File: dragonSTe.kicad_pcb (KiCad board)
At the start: 2 copper layers, 130 parts, among them J2 MIDI OUT, J3 MIDI IN, J4 DB25_Socket, J5 DB25_Pins, J6 Keyboard, SW1 RESET, U1 68000, U5 LM555xM, U7 MC6850, U8 MC6850, U9 YM2149, X1 8.010613MHz

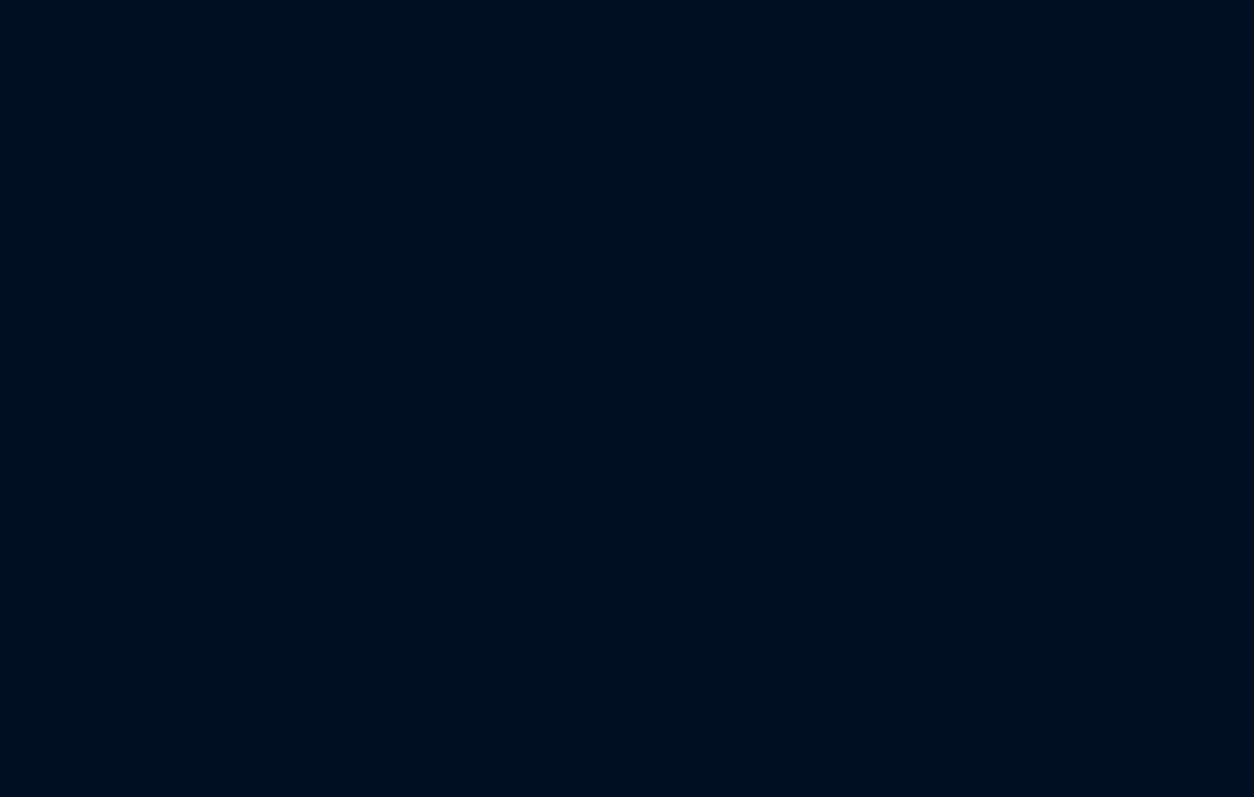
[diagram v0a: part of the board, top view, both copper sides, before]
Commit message: motherboard: Added the HDD and FDD controller logic to the schematic
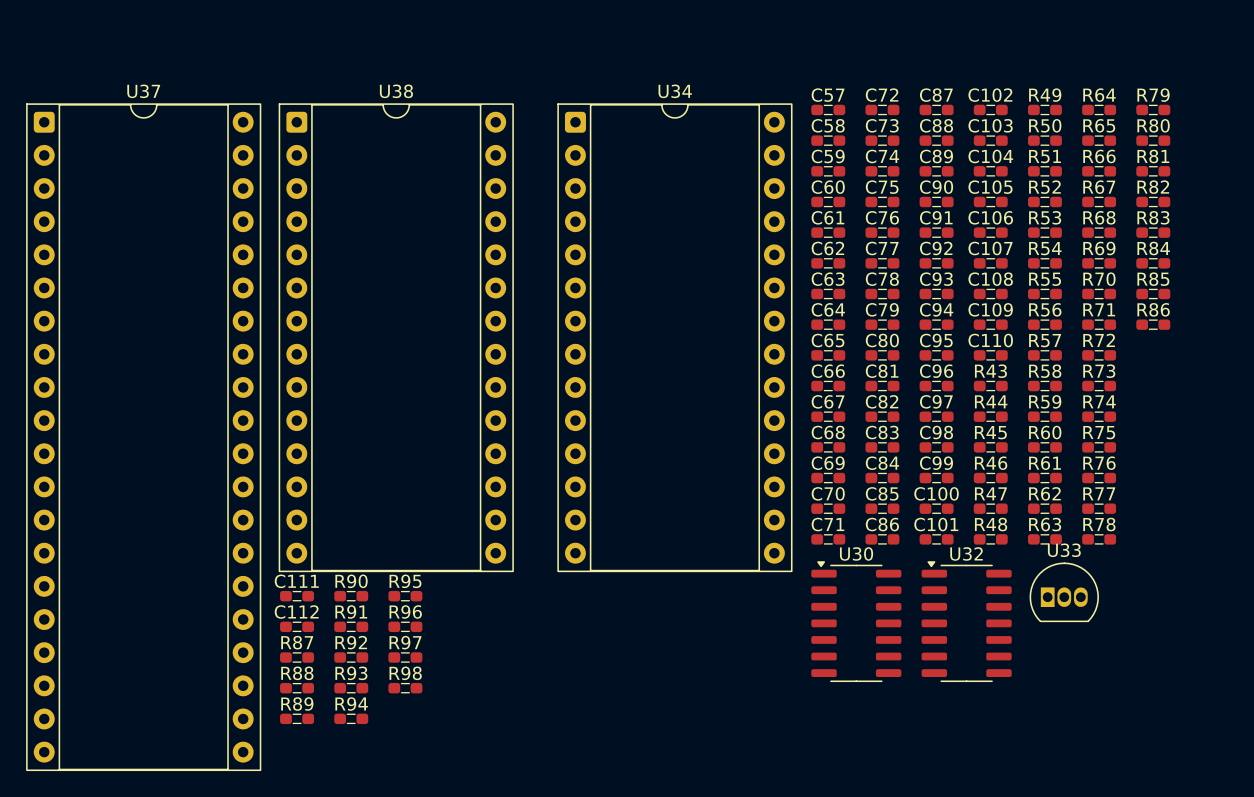
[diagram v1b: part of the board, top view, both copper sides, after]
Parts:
- added C100: 8n2, rhais_rcl:C0603, F.Cu at (156.9, 193.2)
- added C101: 8n2, rhais_rcl:C0603, F.Cu at (156.9, 195.6)
- added C102: 8n2, rhais_rcl:C0603, F.Cu at (161.1, 162.7)
- added C103: 880p, rhais_rcl:C0603, F.Cu at (161.1, 165.0)
- added C104: 880p, rhais_rcl:C0603, F.Cu at (161.1, 167.4)
- added C105: 10n, rhais_rcl:C0603, F.Cu at (161.1, 169.7)
- added C106: 10n, rhais_rcl:C0603, F.Cu at (161.1, 172.1)
- added C107: 10n, rhais_rcl:C0603, F.Cu at (161.1, 174.4)
- added C108: 880p, rhais_rcl:C0603, F.Cu at (161.1, 176.8)
- added C109: 10n, rhais_rcl:C0603, F.Cu at (161.1, 179.1)
- added C110: 880p, rhais_rcl:C0603, F.Cu at (161.1, 181.5)
- added C111: 100n, rhais_rcl:C0603, F.Cu at (108.0, 199.9)
- added C112: 100n, rhais_rcl:C0603, F.Cu at (108.0, 202.3)
- added C57: 100n, rhais_rcl:C0603, F.Cu at (148.7, 162.7)
- added C58: 100n, rhais_rcl:C0603, F.Cu at (148.7, 165.0)
- added C59: 100n, rhais_rcl:C0603, F.Cu at (148.7, 167.4)
- added C60: 100n, rhais_rcl:C0603, F.Cu at (148.7, 169.7)
- added C61: 47u, rhais_rcl:C0603, F.Cu at (148.7, 172.1)
- added C62: 100u, rhais_rcl:C0603, F.Cu at (148.7, 174.4)
- added C63: 100n, rhais_rcl:C0603, F.Cu at (148.7, 176.8)
- added C64: 100u, rhais_rcl:C0603, F.Cu at (148.7, 179.1)
- added C65: 100n, rhais_rcl:C0603, F.Cu at (148.7, 181.5)
- added C66: 10n, rhais_rcl:C0603, F.Cu at (148.7, 183.8)
- added C67: 100n, rhais_rcl:C0603, F.Cu at (148.7, 186.2)
- added C68: 100n, rhais_rcl:C0603, F.Cu at (148.7, 188.5)
- added C69: 100n, rhais_rcl:C0603, F.Cu at (148.7, 190.9)
- added C70: 100n, rhais_rcl:C0603, F.Cu at (148.7, 193.2)
- added C71: 10n, rhais_rcl:C0603, F.Cu at (148.7, 195.6)
- added C72: 100n, rhais_rcl:C0603, F.Cu at (152.8, 162.7)
- added C73: 100n, rhais_rcl:C0603, F.Cu at (152.8, 165.0)
- added C74: 47u, rhais_rcl:C0603, F.Cu at (152.8, 167.4)
- added C75: 1n, rhais_rcl:C0603, F.Cu at (152.8, 169.7)
- added C76: 1n, rhais_rcl:C0603, F.Cu at (152.8, 172.1)
- added C77: 1n, rhais_rcl:C0603, F.Cu at (152.8, 174.4)
- added C78: 1n, rhais_rcl:C0603, F.Cu at (152.8, 176.8)
- added C79: 47u, rhais_rcl:C0603, F.Cu at (152.8, 179.1)
- added C80: 1n, rhais_rcl:C0603, F.Cu at (152.8, 181.5)
- added C81: 1n, rhais_rcl:C0603, F.Cu at (152.8, 183.8)
- added C82: 1n, rhais_rcl:C0603, F.Cu at (152.8, 186.2)
- added C83: 1n, rhais_rcl:C0603, F.Cu at (152.8, 188.5)
- added C84: 47u, rhais_rcl:C0603, F.Cu at (152.8, 190.9)
- added C85: 100n, rhais_rcl:C0603, F.Cu at (152.8, 193.2)
- added C86: 100n, rhais_rcl:C0603, F.Cu at (152.8, 195.6)
- added C87: 47u, rhais_rcl:C0603, F.Cu at (156.9, 162.7)
- added C88: 47u, rhais_rcl:C0603, F.Cu at (156.9, 165.0)
- added C89: 10u, rhais_rcl:C0603, F.Cu at (156.9, 167.4)
- added C90: 47u, rhais_rcl:C0603, F.Cu at (156.9, 169.7)
- added C91: 47u, rhais_rcl:C0603, F.Cu at (156.9, 172.1)
- added C92: 47u, rhais_rcl:C0603, F.Cu at (156.9, 174.4)
- added C93: 47u, rhais_rcl:C0603, F.Cu at (156.9, 176.8)
- added C94: 100n, rhais_rcl:C0603, F.Cu at (156.9, 179.1)
- added C95: 100u, rhais_rcl:C0603, F.Cu at (156.9, 181.5)
- added C96: 100n, rhais_rcl:C0603, F.Cu at (156.9, 183.8)
- added C97: 47u, rhais_rcl:C0603, F.Cu at (156.9, 186.2)
- added C98: 47u, rhais_rcl:C0603, F.Cu at (156.9, 188.5)
- added C99: 8n2, rhais_rcl:C0603, F.Cu at (156.9, 190.9)
- added R43: 10k, rhais_rcl:R0603, F.Cu at (161.1, 183.8)
- added R44: 10k, rhais_rcl:R0603, F.Cu at (161.1, 186.2)
- added R45: 8k2, rhais_rcl:R0603, F.Cu at (161.1, 188.5)
- added R46: 8k2, rhais_rcl:R0603, F.Cu at (161.1, 190.9)
- added R47: 100k, rhais_rcl:R0603, F.Cu at (161.1, 193.2)
- added R48: 10R, rhais_rcl:R0603, F.Cu at (161.1, 195.6)
- added R49: 10R, rhais_rcl:R0603, F.Cu at (165.2, 162.7)
- added R50: 10k, rhais_rcl:R0603, F.Cu at (165.2, 165.0)
- added R51: 10k, rhais_rcl:R0603, F.Cu at (165.2, 167.4)
- added R52: 8k2, rhais_rcl:R0603, F.Cu at (165.2, 169.7)
- added R53: 8k2, rhais_rcl:R0603, F.Cu at (165.2, 172.1)
- added R54: 100k, rhais_rcl:R0603, F.Cu at (165.2, 174.4)
- added R55: 10k, rhais_rcl:R0603, F.Cu at (165.2, 176.8)
- added R56: 10k, rhais_rcl:R0603, F.Cu at (165.2, 179.1)
- added R57: 10k, rhais_rcl:R0603, F.Cu at (165.2, 181.5)
- added R58: 10k, rhais_rcl:R0603, F.Cu at (165.2, 183.8)
- added R59: 1k8, rhais_rcl:R0603, F.Cu at (165.2, 186.2)
- added R60: 10k, rhais_rcl:R0603, F.Cu at (165.2, 188.5)
- added R61: 10k, rhais_rcl:R0603, F.Cu at (165.2, 190.9)
- added R62: 10k, rhais_rcl:R0603, F.Cu at (165.2, 193.2)
- added R63: 10k, rhais_rcl:R0603, F.Cu at (165.2, 195.6)
- added R64: 1k8, rhais_rcl:R0603, F.Cu at (169.4, 162.7)
- added R65: 10k, rhais_rcl:R0603, F.Cu at (169.4, 165.0)
- added R66: 3k6, rhais_rcl:R0603, F.Cu at (169.4, 167.4)
- added R67: 1k, rhais_rcl:R0603, F.Cu at (169.4, 169.7)
- added R68: 10k, rhais_rcl:R0603, F.Cu at (169.4, 172.1)
- added R69: 3k6, rhais_rcl:R0603, F.Cu at (169.4, 174.4)
- added R70: 1k, rhais_rcl:R0603, F.Cu at (169.4, 176.8)
- added R71: 1k, rhais_rcl:R0603, F.Cu at (169.4, 179.1)
- added R72: 1k, rhais_rcl:R0603, F.Cu at (169.4, 181.5)
- added R73: 270k, rhais_rcl:R0603, F.Cu at (169.4, 183.8)
- added R74: 270k, rhais_rcl:R0603, F.Cu at (169.4, 186.2)
- added R75: 51k, rhais_rcl:R0603, F.Cu at (169.4, 188.5)
- added R76: 51k, rhais_rcl:R0603, F.Cu at (169.4, 190.9)
- added R77: 10k, rhais_rcl:R0603, F.Cu at (169.4, 193.2)
- added R78: 10k, rhais_rcl:R0603, F.Cu at (169.4, 195.6)
- added R79: 470R, rhais_rcl:R0603, F.Cu at (173.6, 162.7)
- added R80: 470R, rhais_rcl:R0603, F.Cu at (173.6, 165.0)
- added R81: 1M, rhais_rcl:R0603, F.Cu at (173.6, 167.4)
- added R82: 1M, rhais_rcl:R0603, F.Cu at (173.6, 169.7)
- added R83: 1M, rhais_rcl:R0603, F.Cu at (173.6, 172.1)
- added R84: 470R, rhais_rcl:R0603, F.Cu at (173.6, 174.4)
- added R85: 1M, rhais_rcl:R0603, F.Cu at (173.6, 176.8)
- added R86: 470R, rhais_rcl:R0603, F.Cu at (173.6, 179.1)
- added R87: 1k, rhais_rcl:R0603, F.Cu at (108.0, 204.6)
- added R88: 1k, rhais_rcl:R0603, F.Cu at (108.0, 207.0)
- added R89: 1k, rhais_rcl:R0603, F.Cu at (108.0, 209.3)
- added R90: 1k, rhais_rcl:R0603, F.Cu at (112.1, 199.9)
- added R91: 1k, rhais_rcl:R0603, F.Cu at (112.1, 202.3)
- added R92: 1k, rhais_rcl:R0603, F.Cu at (112.1, 204.6)
- added R93: 1k, rhais_rcl:R0603, F.Cu at (112.1, 207.0)
- added R94: 220R, rhais_rcl:R0603, F.Cu at (112.1, 209.3)
- added R95: 47R, rhais_rcl:R0603, F.Cu at (116.2, 199.9)
- added R96: 47R, rhais_rcl:R0603, F.Cu at (116.2, 202.3)
- added R97: 47R, rhais_rcl:R0603, F.Cu at (116.2, 204.6)
- added R98: 47R, rhais_rcl:R0603, F.Cu at (116.2, 207.0)
- added U30: LF347DT, Package_SO:SO-14_3.9x8.65mm_P1.27mm, F.Cu at (150.8, 202.0)
- added U32: LF347DT, Package_SO:SO-14_3.9x8.65mm_P1.27mm, F.Cu at (159.2, 202.0)
- added U33: LM78L82, Package_TO_SOT_THT:TO-92_Inline, F.Cu at (165.5, 200.0)
- added U34: LMC1992, Package_DIP:DIP-28_W15.24mm_Socket, F.Cu at (129.3, 163.6)
- added U37: DMA, Package_DIP:DIP-40_W15.24mm_Socket, F.Cu at (88.6, 163.6)
- added U38: WD1772, Package_DIP:DIP-28_W15.24mm_Socket, F.Cu at (107.9, 163.6)
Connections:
- net /Disk & DMA/BD0SEL renamed /Disk & Floppy/BD0SEL
- net /Disk & DMA/CLK2 renamed /Disk & Floppy/CLK2
- net /Disk & DMA/D0SEL renamed /Disk & Floppy/D0SEL
- net /Disk & DMA/D1SEL renamed /Disk & Floppy/D1SEL
- net /Disk & DMA/S0SEL renamed /Disk & Floppy/S0SEL
- net Net-(U9-A) renamed /DAC + Joysticks/AUDIOS
- net VCC renamed +5V
- RN13 pad 1: unconnected-(RN13-R1.1-Pad1) -> Net-(RN13-R1.1)
- RN13 pad 2: unconnected-(RN13-R2.1-Pad2) -> Net-(RN13-R2.1)
- RN13 pad 3: unconnected-(RN13-R3.1-Pad3) -> Net-(RN13-R3.1)
- RN13 pad 4: unconnected-(RN13-R4.1-Pad4) -> Net-(RN13-R4.1)
- RN14 pad 1: unconnected-(RN14-R1.1-Pad1) -> Net-(RN14-R1.1)
- RN14 pad 2: unconnected-(RN14-R2.1-Pad2) -> Net-(RN14-R2.1)
- RN14 pad 3: unconnected-(RN14-R3.1-Pad3) -> Net-(RN14-R3.1)
- RN14 pad 4: unconnected-(RN14-R4.1-Pad4) -> Net-(RN14-R4.1)
- RN15 pad 1: unconnected-(RN15-R1.1-Pad1) -> /Disk & Floppy/~{HDCS}
- RN15 pad 2: unconnected-(RN15-R2.1-Pad2) -> /Disk & Floppy/~{HDACK}
- RN15 pad 3: unconnected-(RN15-R3.1-Pad3) -> /Disk & Floppy/HDA0
- RN15 pad 4: unconnected-(RN15-R4.1-Pad4) -> /Disk & Floppy/HDR/~{W}
- X1 pad 3: /Disk & DMA/SCLK -> /Disk & Floppy/SCLK

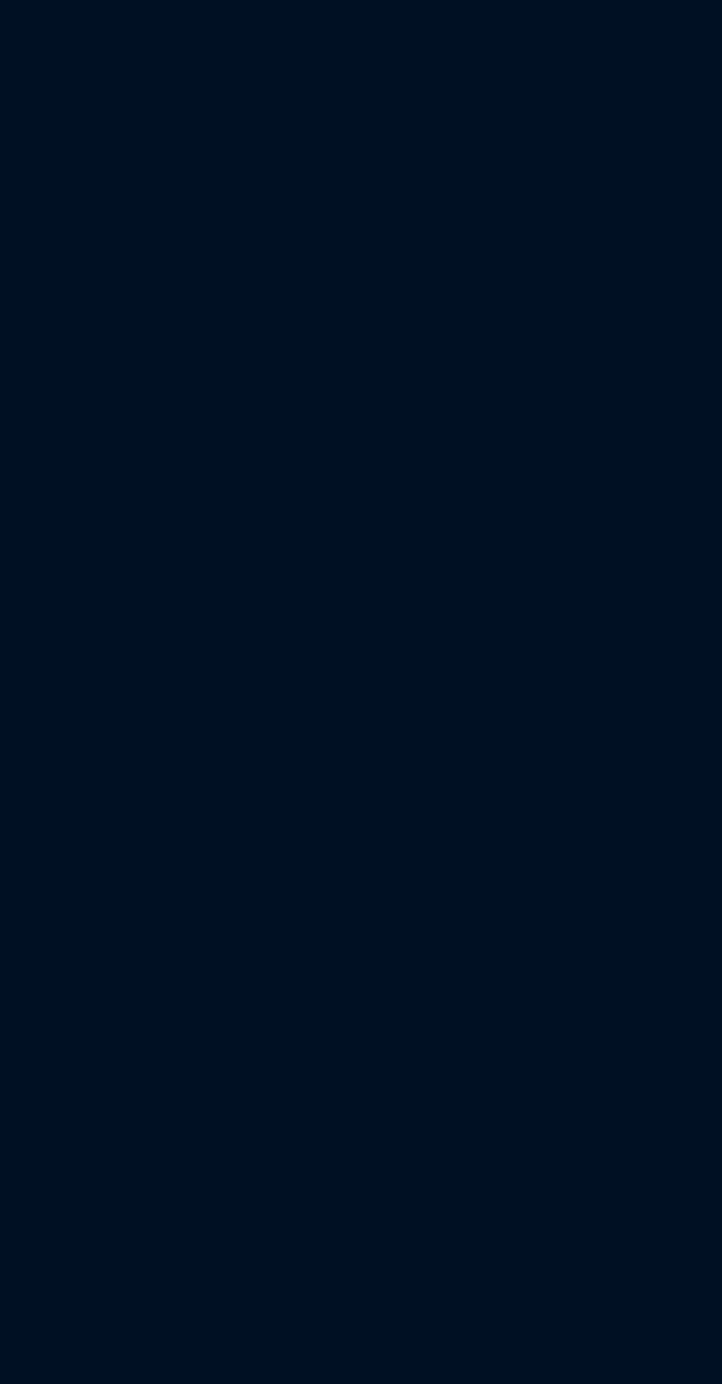
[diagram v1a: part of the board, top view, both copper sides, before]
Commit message: motherboard: Added the BLiTTER to the schematic and tidied up a pile
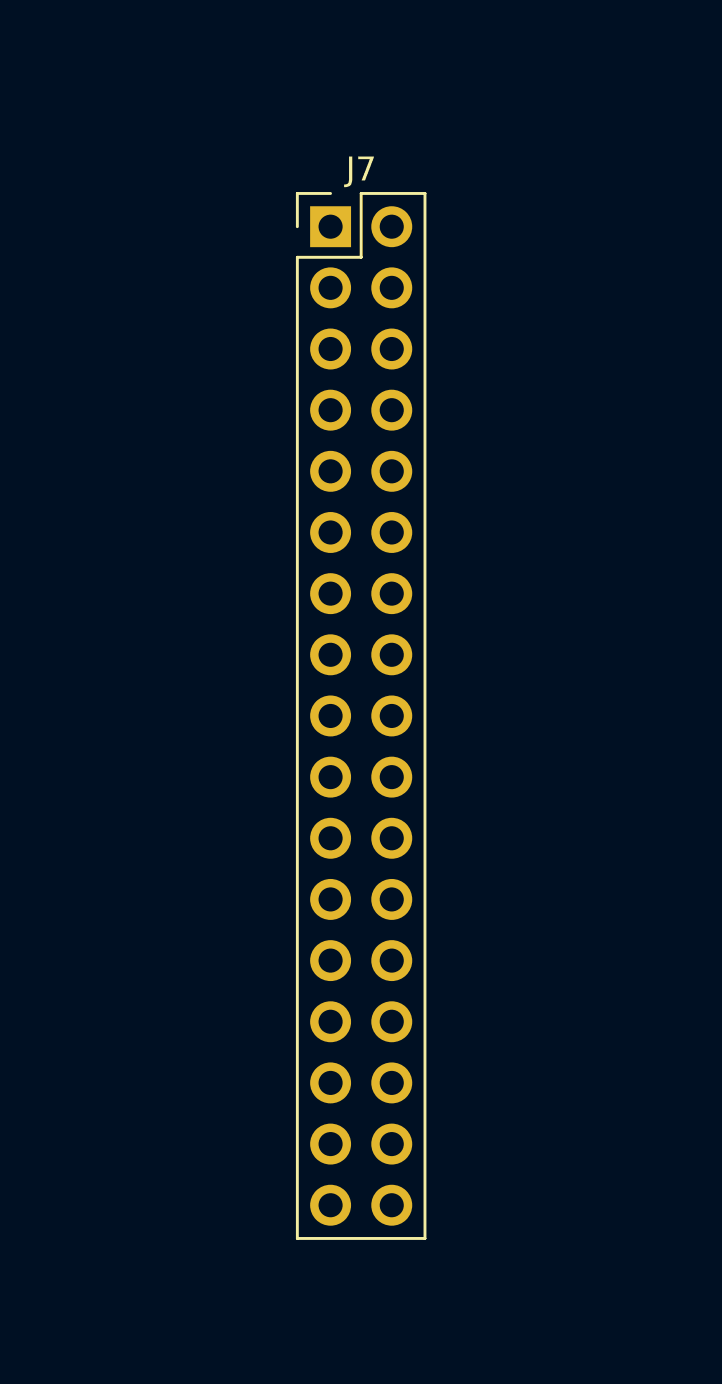
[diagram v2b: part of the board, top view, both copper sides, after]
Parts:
- added J7: Internal FDD, Connector_PinHeader_2.54mm:PinHeader_2x17_P2.54mm_Vertical, F.Cu at (198.7, 157.4)

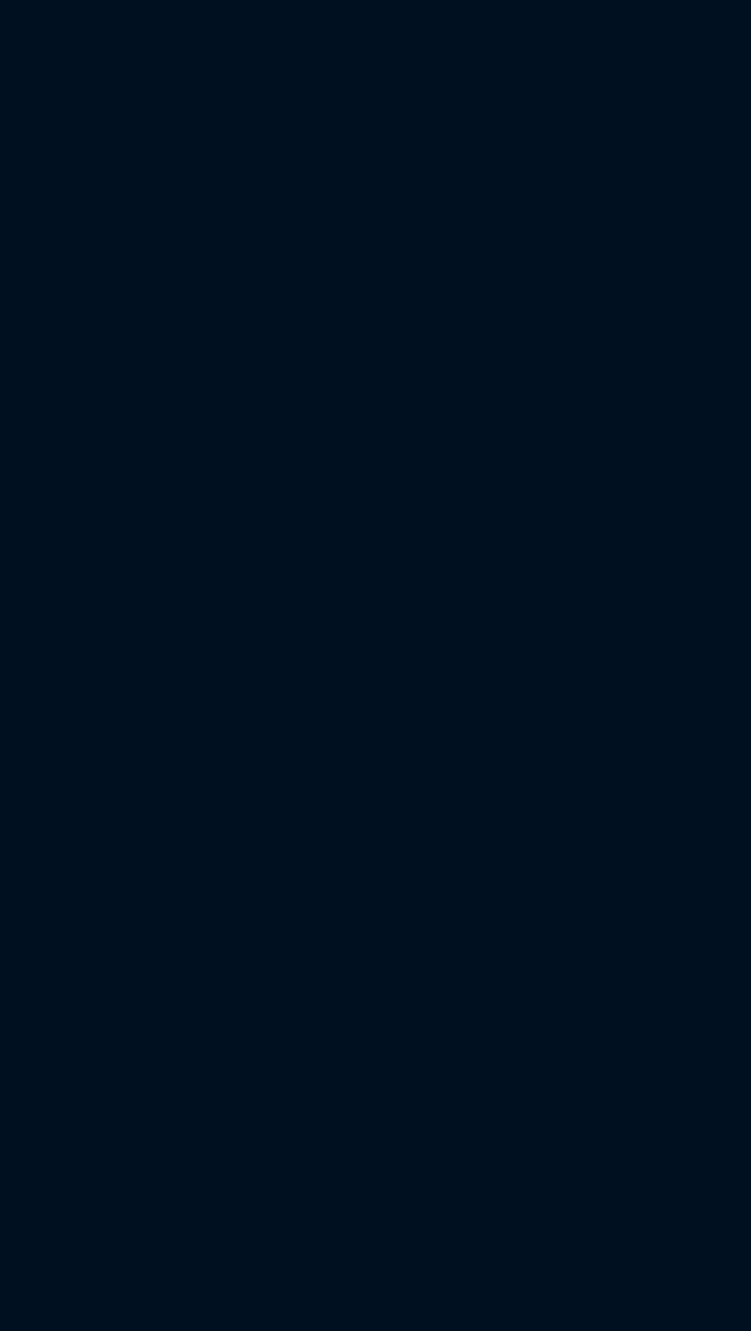
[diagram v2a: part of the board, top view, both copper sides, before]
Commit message: motherboard: Added SHIFTER to the schematic and tidied up a pile
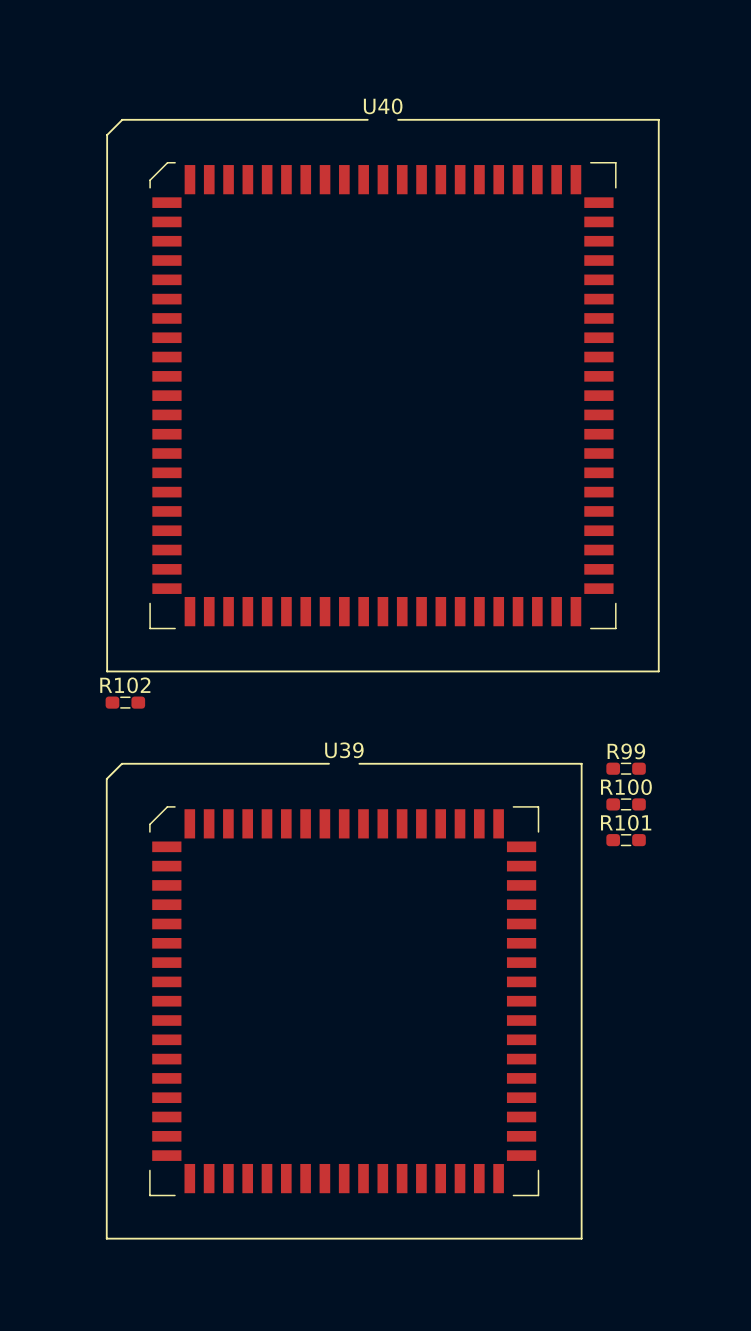
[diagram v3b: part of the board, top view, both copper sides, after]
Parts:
- added R100: 10k, rhais_rcl:R0603, F.Cu at (303.9, 162.2)
- added R101: 10k, rhais_rcl:R0603, F.Cu at (303.9, 164.5)
- added R102: 1k, rhais_rcl:R0603, F.Cu at (270.9, 155.5)
- added R99: 10k, rhais_rcl:R0603, F.Cu at (303.9, 159.8)
- added U39: STB, Package_LCC:PLCC-68_SMD-Socket, F.Cu at (285.3, 175.1)
- added U40: GST_SHIFTER, Package_LCC:PLCC-84_SMD-Socket, F.Cu at (287.9, 135.3)
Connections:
- R34 pad 2: /IO Interfaces/~{BLT_INT} -> /CPU+ROMs/~{BLT_INT}
- U1 pad 11: unconnected-(U1-BG-Pad11) -> /CPU+ROMs/~{CPU_BG}
- U1 pad 26: unconnected-(U1-FC2-Pad26) -> /CPU+ROMs/FC2
- U1 pad 27: unconnected-(U1-FC1-Pad27) -> /CPU+ROMs/FC1
- U1 pad 28: unconnected-(U1-FC0-Pad28) -> /CPU+ROMs/FC0
- U37 pad 1: /CPU+ROMs/SysBus.R/~{W} -> /Disk & Floppy/SysBus.R/~{W}
- U37 pad 12: /CPU+ROMs/SysBus.D8 -> /Disk & Floppy/SysBus.D8
- U37 pad 13: /CPU+ROMs/SysBus.D9 -> /Disk & Floppy/SysBus.D9
- U37 pad 14: /CPU+ROMs/SysBus.D10 -> /Disk & Floppy/SysBus.D10
- U37 pad 15: /CPU+ROMs/SysBus.D11 -> /Disk & Floppy/SysBus.D11
- U37 pad 16: /CPU+ROMs/SysBus.D12 -> /Disk & Floppy/SysBus.D12
- U37 pad 17: /CPU+ROMs/SysBus.D13 -> /Disk & Floppy/SysBus.D13
- U37 pad 18: /CPU+ROMs/SysBus.D14 -> /Disk & Floppy/SysBus.D14
- U37 pad 19: /CPU+ROMs/SysBus.D15 -> /Disk & Floppy/SysBus.D15
- U37 pad 2: /CPU+ROMs/SysBus.A1 -> /Disk & Floppy/SysBus.A1
- U7 pad 11: /CPU+ROMs/SysBus.A1 -> /IO Interfaces/SysBus.A1
- U7 pad 13: /CPU+ROMs/SysBus.R/~{W} -> /IO Interfaces/SysBus.R/~{W}
- U7 pad 14: /CPU+ROMs/SysBus.E -> /IO Interfaces/SysBus.E
- U7 pad 15: /CPU+ROMs/SysBus.D15 -> /IO Interfaces/SysBus.D15
- U7 pad 16: /CPU+ROMs/SysBus.D14 -> /IO Interfaces/SysBus.D14
- U7 pad 17: /CPU+ROMs/SysBus.D13 -> /IO Interfaces/SysBus.D13
- U7 pad 18: /CPU+ROMs/SysBus.D12 -> /IO Interfaces/SysBus.D12
- U7 pad 19: /CPU+ROMs/SysBus.D11 -> /IO Interfaces/SysBus.D11
- U7 pad 20: /CPU+ROMs/SysBus.D10 -> /IO Interfaces/SysBus.D10
- U7 pad 21: /CPU+ROMs/SysBus.D9 -> /IO Interfaces/SysBus.D9
- U7 pad 22: /CPU+ROMs/SysBus.D8 -> /IO Interfaces/SysBus.D8
- U7 pad 9: /CPU+ROMs/SysBus.A2 -> /IO Interfaces/SysBus.A2
- U8 pad 10: /CPU+ROMs/SysBus.A2 -> /IO Interfaces/SysBus.A2
- U8 pad 11: /CPU+ROMs/SysBus.A1 -> /IO Interfaces/SysBus.A1
- U8 pad 13: /CPU+ROMs/SysBus.R/~{W} -> /IO Interfaces/SysBus.R/~{W}
- U8 pad 14: /CPU+ROMs/SysBus.E -> /IO Interfaces/SysBus.E
- U8 pad 15: /CPU+ROMs/SysBus.D15 -> /IO Interfaces/SysBus.D15
- U8 pad 16: /CPU+ROMs/SysBus.D14 -> /IO Interfaces/SysBus.D14
- U8 pad 17: /CPU+ROMs/SysBus.D13 -> /IO Interfaces/SysBus.D13
- U8 pad 18: /CPU+ROMs/SysBus.D12 -> /IO Interfaces/SysBus.D12
- U8 pad 19: /CPU+ROMs/SysBus.D11 -> /IO Interfaces/SysBus.D11
- U8 pad 20: /CPU+ROMs/SysBus.D10 -> /IO Interfaces/SysBus.D10
- U8 pad 21: /CPU+ROMs/SysBus.D9 -> /IO Interfaces/SysBus.D9
- U8 pad 22: /CPU+ROMs/SysBus.D8 -> /IO Interfaces/SysBus.D8
- U9 pad 30: /CPU+ROMs/SysBus.D15 -> /IO Interfaces/SysBus.D15
- U9 pad 31: /CPU+ROMs/SysBus.D14 -> /IO Interfaces/SysBus.D14
- U9 pad 32: /CPU+ROMs/SysBus.D13 -> /IO Interfaces/SysBus.D13
- U9 pad 33: /CPU+ROMs/SysBus.D12 -> /IO Interfaces/SysBus.D12
- U9 pad 34: /CPU+ROMs/SysBus.D11 -> /IO Interfaces/SysBus.D11
- U9 pad 35: /CPU+ROMs/SysBus.D10 -> /IO Interfaces/SysBus.D10
- U9 pad 36: /CPU+ROMs/SysBus.D9 -> /IO Interfaces/SysBus.D9
- U9 pad 37: /CPU+ROMs/SysBus.D8 -> /IO Interfaces/SysBus.D8
